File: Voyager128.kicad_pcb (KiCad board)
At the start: 2 copper layers, 71.6 x 35.7 mm, 22 parts, among them J1 AppleIIBus, U1 74HCT245, U2 LY621024, U3 GAL22V10, U4 74LS125

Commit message: Board done but ugly
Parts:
- removed C2, C5: 2u2, stdpads:C_0805
- removed FID3: Fiducial, stdpads:Fiducial
- removed H3: , stdpads:PasteHole_1.1mm_PTH
- added C10: 2u2, stdpads:C_0603, F.Cu at (126.3, 124.8)
- added C12: 2u2, stdpads:C_0603, F.Cu at (130.7, 108.8)
- added C13: 2u2, stdpads:C_0603, F.Cu at (104.3, 112.4)
- added C15: 2u2, stdpads:C_0603, F.Cu at (122.2, 108.8)
- added C7: 2u2, stdpads:C_0603, F.Cu at (100.7, 124.8)
- added C8: 2u2, stdpads:C_0603, F.Cu at (108.0, 124.8)
- added C9: 2u2, stdpads:C_0603, F.Cu at (115.2, 124.8)
- added U10: 74LS32, stdpads:TSSOP-14_4.4x5mm_P0.65mm, F.Cu at (128.5, 112.5)
- added U11: 74AHC1G126GW, stdpads:SOT-353, F.Cu at (118.3, 122.7)
- added U5: 74LS04, stdpads:TSSOP-14_4.4x5mm_P0.65mm, F.Cu at (89.8, 122.6)
- added U6: 74LS08, stdpads:TSSOP-14_4.4x5mm_P0.65mm, F.Cu at (97.2, 122.6)
- added U7: 74LS08, stdpads:TSSOP-14_4.4x5mm_P0.65mm, F.Cu at (104.5, 122.6)
- added U8: 74LS08, stdpads:TSSOP-14_4.4x5mm_P0.65mm, F.Cu at (111.8, 122.6)
- added U9: 74LS08, stdpads:TSSOP-14_4.4x5mm_P0.65mm, F.Cu at (122.8, 122.6)
- C3, C4, C6: footprint stdpads:C_0805 -> stdpads:C_0603
- R1: value 1k -> 3k3
- U1: value 74HCT245 -> 621024; footprint stdpads:SOIC-20W_7.5mm -> stdpads:TSOP-I-32_18.4x8mm_P0.5mm
- U2: value LY621024 -> 74HCT245; footprint stdpads:SOP-32_P1.27mm -> stdpads:TSSOP-20_4.4x6.5mm_P0.65mm
- U3: value GAL22V10 -> 74LS174; footprint stdpads:PLCC-28 -> stdpads:TSSOP-16_4.4x5mm_P0.65mm
- U4: value 74LS125 -> 74LS174; footprint stdpads:SOIC-14_3.9mm -> stdpads:TSSOP-16_4.4x5mm_P0.65mm
- moved C3 37.2 mm to (86.0, 124.8), turned to 90 degrees
- moved C4 21.6 mm to (113.5, 108.8)
- moved U2 21.2 mm to (81.7, 122.6)
- moved C6 15.5 mm to (93.3, 124.8)
- moved U4 14.6 mm to (120.0, 112.5), turned to 270 degrees
- moved U3 10.5 mm to (111.3, 112.5), turned to 270 degrees
- moved R1 6.07 mm to (118.3, 125.5)
- moved U1 6.01 mm to (92.1, 112.2)
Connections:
- U1 pad 1: /R~WE~ -> /A0
- U1 pad 10: GND -> /RA16
- U1 pad 11: /D0 -> /RA15
- U1 pad 12: /D1 -> /RA14
- U1 pad 13: /D2 -> /A6
- U1 pad 14: /D3 -> /RA12
- U1 pad 15: /D4 -> /A5
- U1 pad 16: /D5 -> /A4
- U1 pad 17: /D6 -> /A8
- U1 pad 18: /D7 -> /A9
- U1 pad 19: /R~CS~ -> /A10
- U1 pad 2: /RD0 -> /A1
- U1 pad 20: +5V -> /A11
- U1 pad 3: /RD1 -> /A2
- U1 pad 4: /RD2 -> /A3
- U1 pad 5: /RD3 -> /R~WE~
- U1 pad 6: /RD4 -> +5V
- U1 pad 7: /RD5 -> /A7
- U1 pad 8: /RD6 -> +5V
- U1 pad 9: /RD7 -> Net-(U1-Pad9)
- U2 pad 1: Net-(U2-Pad1) -> /R~WE~
- U2 pad 10: /A8 -> GND
- U2 pad 11: /A7 -> /D0
- U2 pad 12: /A6 -> /D1
- U2 pad 13: /RD3 -> /D2
- U2 pad 14: /RD2 -> /D3
- U2 pad 15: /RD1 -> /D4
- U2 pad 16: GND -> /D5
- U2 pad 17: /RD0 -> /D6
- U2 pad 18: /RD7 -> /D7
- U2 pad 19: /RD6 -> /R~CS~
- U2 pad 2: /RA16 -> /RD3
- U2 pad 20: /RD5 -> +5V
- U2 pad 3: /RA15 -> /RD2
- U2 pad 4: /RA14 -> /RD1
- U2 pad 5: /A13 -> /RD0
- U2 pad 6: /RA12 -> /RD7
- U2 pad 7: /A11 -> /RD6
- U2 pad 8: /A10 -> /RD5
- U2 pad 9: /A9 -> /RD4
- U3 pad 1: (no net) -> /~RES~
- U3 pad 10: /A13 -> Net-(U3-Pad10)
- U3 pad 11: /A14 -> Net-(U3-Pad11)
- U3 pad 12: /A15 -> Net-(U3-Pad12)
- U3 pad 13: /R~WE~ -> Net-(U3-Pad13)
- U3 pad 14: GND -> Net-(U3-Pad14)
- U3 pad 15: (no net) -> Net-(U3-Pad15)
- U3 pad 16: /~RES~ -> +5V
- U3 pad 2: /~DEVSEL~ -> /RA14
- U3 pad 3: /PHI1 -> /A0
- U3 pad 4: /A0 -> /A1
- U3 pad 5: /A1 -> /RA15
- U3 pad 6: /A2 -> /A3
- U3 pad 7: /A3 -> /RA16
- U3 pad 8: (no net) -> GND
- U3 pad 9: /A12 -> /~DEV~andA2
- U4 pad 1: GND -> /~RES~
- U4 pad 11: Net-(U4-Pad10) -> Net-(U4-Pad11)
- U4 pad 12: Net-(U4-Pad12) -> /ENWR
- U4 pad 13: GND -> /ENWR1A0
- U4 pad 14: +5V -> Net-(U4-Pad14)
- U4 pad 2: /R~CS~1 -> /ENRD
- U4 pad 3: /R~CS~ -> /~A0XOR1~
- U4 pad 4: GND -> /A3
- U4 pad 5: /~INH~b -> /BankAB
- U4 pad 6: Net-(U4-Pad12) -> /A0
- U4 pad 7: GND -> /ENWR1
- U4 pad 8: /~INH~ -> GND
- U4 pad 9: GND -> /~DEV~and~A2~
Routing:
- net +5V: track 307.8 -> 65.9 mm, vias 18 -> 51
- net /A13: track 20.4 -> 91.6 mm, vias 2 -> 6
- net /A0: track 51.8 -> 117.3 mm, vias 2 -> 4
- net /R~CS~: track 82.6 -> 19.5 mm
- net /A3: track 38.8 -> 100.9 mm, vias 2 -> 6
- net /~RES~: track 12.5 -> 65.9 mm, vias 1 -> 2
- net /A2: track 41.3 -> 93.7 mm
- net /A1: track 44.9 -> 96.4 mm, vias 2 -> 3
- net /A4: track 17.3 -> 63.4 mm
- net Net-(U10-Pad2): track 0.00 -> 45.8 mm, vias 0 -> 4
- net /PHI1: track 49.5 -> 4.44 mm, vias 1 -> 0
- net /A7: track 27.4 -> 69.9 mm
- net Net-(U10-Pad10): track 0.00 -> 42.3 mm, vias 0 -> 2
- net Net-(U10-Pad1): track 0.00 -> 39.3 mm, vias 0 -> 4
- net /~DEV~and~A2~: track 0.00 -> 38.6 mm, vias 0 -> 2
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- added copper zone on In2.Cu, net +5V
- added copper zone on In1.Cu, net GND
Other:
- copper layers 2 -> 4
- net class Default: clearance 0.1524 -> 0.15; trace_width 0.1524 -> 0.15; via_dia 0.6 -> 0.5; via_drill 0.3 -> 0.2
- rule trace_clearance: 0.1524 -> 0.15
- rule trace_min: 0.1524 -> 0.15
- rule via_min_drill: 0.3 -> 0.2
- rule via_min_size: 0.4 -> 0.5
- board text added: "4208B"
- board text removed: "4208A"
- board text removed: "JLCJLCJLC"
- board text removed: "ZK, GF"

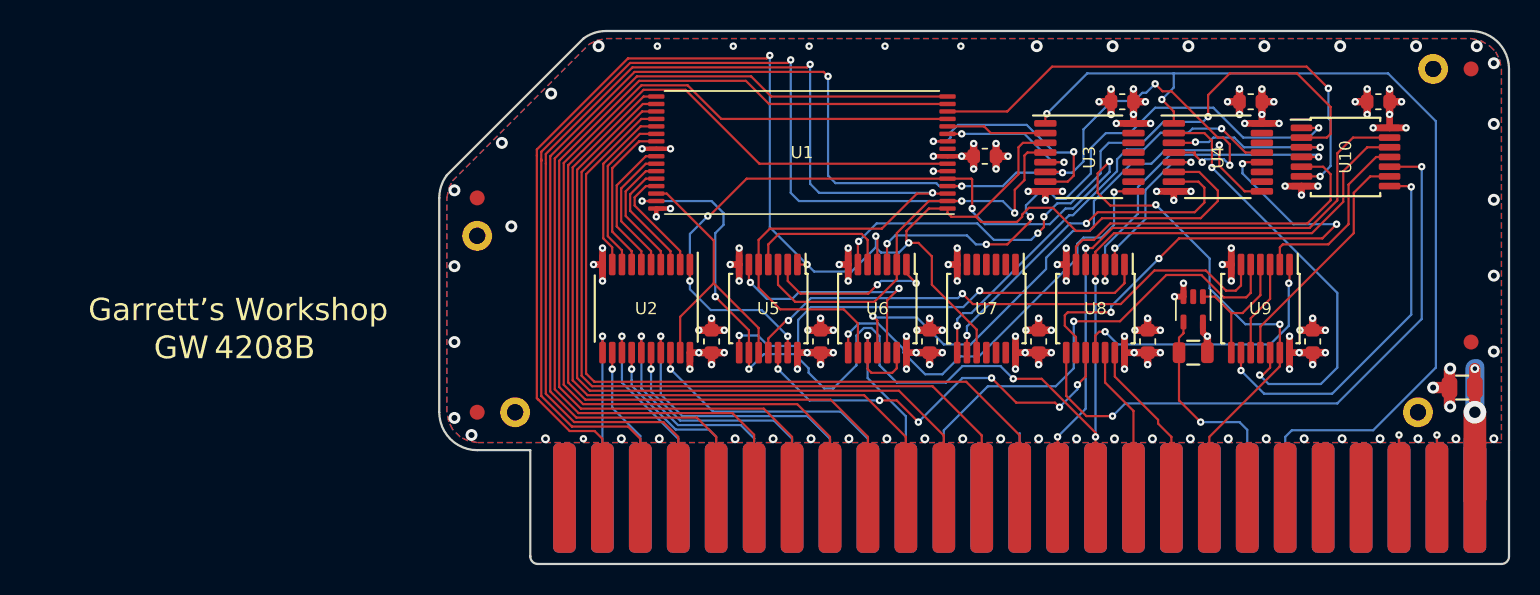
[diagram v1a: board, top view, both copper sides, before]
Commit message: Routing done, needs made pretty
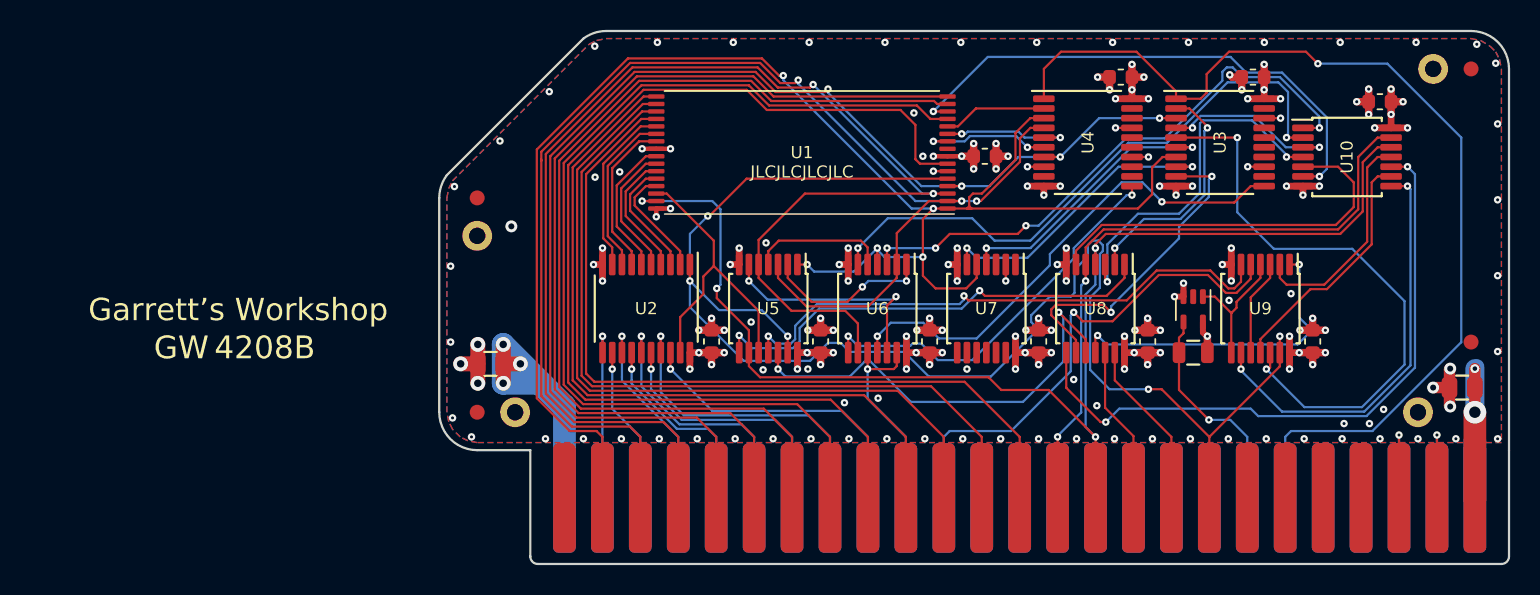
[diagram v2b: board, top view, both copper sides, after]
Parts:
- removed C15, C4: 2u2, stdpads:C_0603
- added C11: 2u2, stdpads:C_0603, F.Cu at (122.3, 107.1)
- added C2: 2u2, stdpads:C_0603, F.Cu at (113.5, 107.1)
- added C5: 2u2, stdpads:C_0805, F.Cu at (71.2, 126.3)
- U3, U4: value 74LS174 -> 74LS273; footprint stdpads:TSSOP-16_4.4x5mm_P0.65mm -> stdpads:TSSOP-20_4.4x6.5mm_P0.65mm
- moved U3 8.81 mm to (120.1, 111.5)
- moved U4 8.76 mm to (111.2, 111.5)
- moved C12 0.10 mm to (130.8, 108.8)
- moved U10 0.10 mm to (128.6, 112.5)
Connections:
- U3 pad 10: Net-(U3-Pad10) -> GND
- U3 pad 11: Net-(U3-Pad11) -> /~DEV~and~A2~
- U3 pad 13: Net-(U3-Pad13) -> GND
- U3 pad 14: Net-(U3-Pad14) -> GND
- U3 pad 16: +5V -> Net-(U3-Pad16)
- U3 pad 2: /RA14 -> /BankAB
- U3 pad 3: /A0 -> /A3
- U3 pad 4: /A1 -> /~A0XOR1~
- U3 pad 5: /RA15 -> /ENRD
- U3 pad 6: /A3 -> /ENWR1
- U3 pad 7: /RA16 -> /A0
- U3 pad 8: GND -> /ENWR1A0
- U3 pad 9: /~DEV~andA2 -> /ENWR
- U4 pad 10: Net-(U4-Pad10) -> GND
- U4 pad 11: Net-(U4-Pad11) -> /~DEV~andA2
- U4 pad 12: /ENWR -> Net-(U4-Pad12)
- U4 pad 13: /ENWR1A0 -> GND
- U4 pad 14: Net-(U4-Pad14) -> GND
- U4 pad 16: +5V -> Net-(U4-Pad16)
- U4 pad 2: /ENRD -> /RA14
- U4 pad 3: /~A0XOR1~ -> /A0
- U4 pad 4: /A3 -> /A1
- U4 pad 5: /BankAB -> /RA15
- U4 pad 6: /A0 -> /RA16
- U4 pad 7: /ENWR1 -> /A3
- U4 pad 9: /~DEV~and~A2~ -> Net-(U4-Pad9)
- U7 pad 1: (no net) -> GND
- U7 pad 10: /A0 -> GND
- U7 pad 11: (no net) -> Net-(U7-Pad11)
- U7 pad 12: (no net) -> GND
- U7 pad 13: (no net) -> GND
- U7 pad 2: (no net) -> GND
- U7 pad 3: (no net) -> Net-(U7-Pad3)
- U7 pad 4: (no net) -> /ENWR1
- U7 pad 5: (no net) -> /A0
- U7 pad 6: (no net) -> /ENWR1A0
- U7 pad 8: /ENWR1A0 -> Net-(U7-Pad8)
- U7 pad 9: /ENWR1 -> GND
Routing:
- net +12V: track 0.00 -> 27.3 mm, vias 0 -> 3
- net /R~WE~: track 81.2 -> 102.1 mm, vias 7 -> 5
- net /A3: track 100.9 -> 83.9 mm, vias 6 -> 4
- net /ENWR: track 33.5 -> 22.2 mm, vias 4 -> 2
- net /ENRD: track 29.2 -> 39.8 mm
- net /ENWR1A0: track 29.1 -> 20.1 mm
- net /A0: track 117.3 -> 108.4 mm, vias 4 -> 5
- net GND: track 62.9 -> 70.3 mm, vias 116 -> 142
- net /RA16: track 15.5 -> 8.81 mm
- net /A1: track 96.4 -> 90.2 mm
- net Net-(U10-Pad2): track 45.8 -> 40.2 mm, vias 4 -> 2
- net /ENWR1: track 24.3 -> 18.8 mm
- net /A13: track 91.6 -> 86.2 mm, vias 6 -> 4
- net /A2: track 93.7 -> 88.7 mm
- net /~DEV~and~A2~: track 38.6 -> 33.6 mm
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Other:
- board text added: "JLCJLCJLCJLC"
